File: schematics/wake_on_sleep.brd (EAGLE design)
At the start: 37.5 x 37.5 mm, 30 parts, among them Q1 MMBT3904, Q2 MMBT3904, Q3 MMBT3904, U1 PIC16F1823ST, U2 ADP160, U3 ADXL362

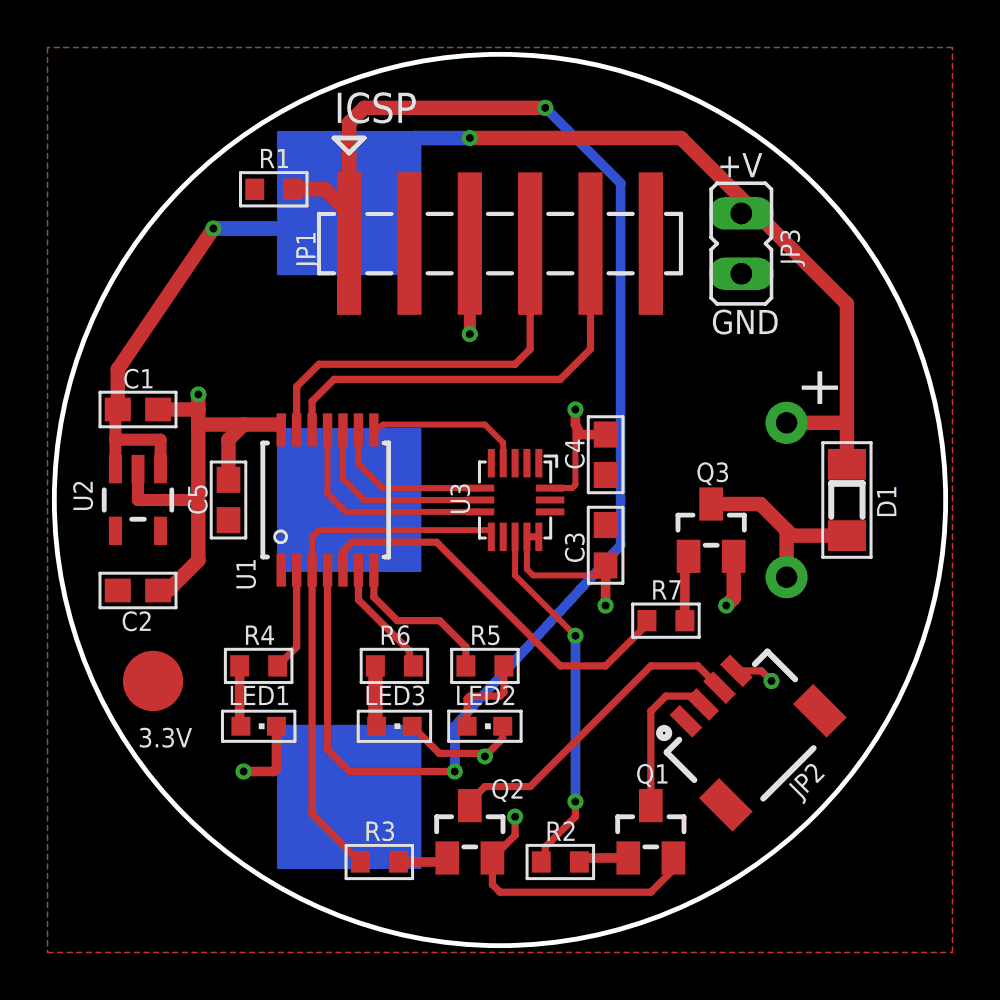
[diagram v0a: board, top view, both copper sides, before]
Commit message: Updated to Rev A.1 and prepared for PCB build
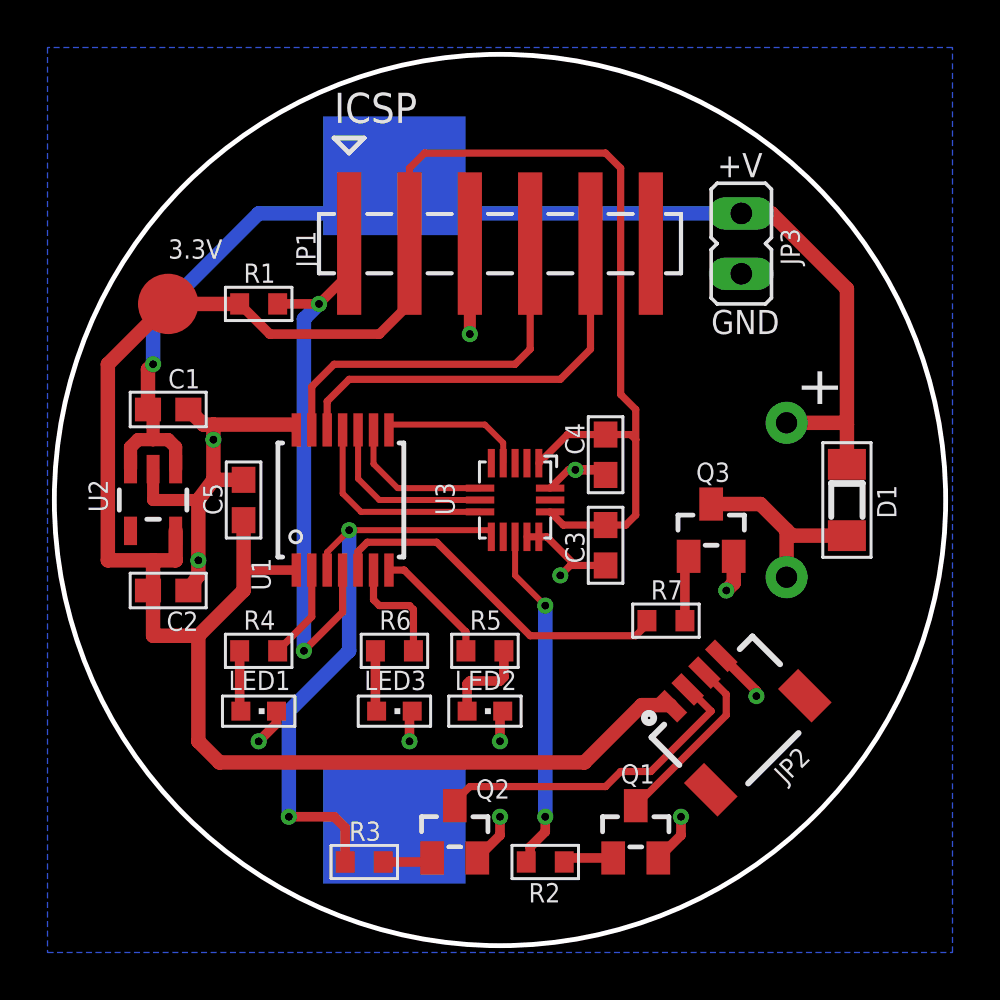
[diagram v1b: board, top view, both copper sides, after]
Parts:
- BAT1: device kevin:BATTCON_20MM -> kevin:BATTCON_20MM_SMD_EJECT
- moved LOGO1 23.1 mm to (26.7, 9.53)
- moved 3.3V 15.9 mm to (5.08, 27.3)
- moved R1 4.87 mm to (8.89, 27.3)
- moved BAT1 1.91 mm to (14.6, 19.1)
- moved C1 1.27 mm to (5.08, 22.9)
- moved C2 1.27 mm to (5.08, 15.2)
- moved JP2 0.90 mm to (27.3, 11.4)
- moved Q2 0.64 mm to (17.1, 5.08)
- moved R2 0.64 mm to (21.0, 3.81)
- moved C5 0.64 mm to (8.26, 19.1)
- moved U2 0.64 mm to (4.45, 19.1)
- moved LED1 0.63 mm to (8.89, 10.2)
- moved LED2 0.63 mm to (18.4, 10.2)
- moved LED3 0.63 mm to (14.6, 10.2)
- moved R3 0.63 mm to (13.3, 3.81)
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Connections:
- net !AWAKE.OUT: now also JP2.2; no longer JP2.3
- net AWAKE.OUT: now also JP2.3; no longer JP2.2
- net GND: now also BAT1.VCC@2; no longer BAT1.2
- net V_BATT: now also BAT1.VCC@1; no longer BAT1.1
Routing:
- net +3V3: track 0.00 -> 109.4 mm
- net !MCLR!/VPP: track 61.7 -> 23.7 mm
- net GND: track 62.3 -> 40.2 mm, vias 9 -> 12
- net !AWAKE.IN: track 22.4 -> 25.4 mm, vias 0 -> 2
- net V_BATT: track 55.9 -> 53.2 mm, vias 2 -> 1
- net BUZZER.OUT: track 17.0 -> 15.3 mm
- net SB0.OUT: track 6.68 -> 5.12 mm
- net AWAKE.OUT: track 6.58 -> 7.56 mm
- net AWAKE.IN: track 15.3 -> 14.5 mm
- net PGC: track 18.3 -> 17.6 mm
- net !CS.OUT: track 9.42 -> 8.78 mm
- net MOSI.OUT: track 6.98 -> 6.34 mm
- net MISO.IN: track 8.20 -> 7.56 mm
- net PGD: track 16.8 -> 16.1 mm
- removed copper zone on layer 1, net +3V3
